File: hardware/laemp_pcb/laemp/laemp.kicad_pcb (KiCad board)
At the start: 2 copper layers, 1 part

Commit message: added new lib and schematic changes
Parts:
- moved A1 116.6 mm to (75.4, 92.8)

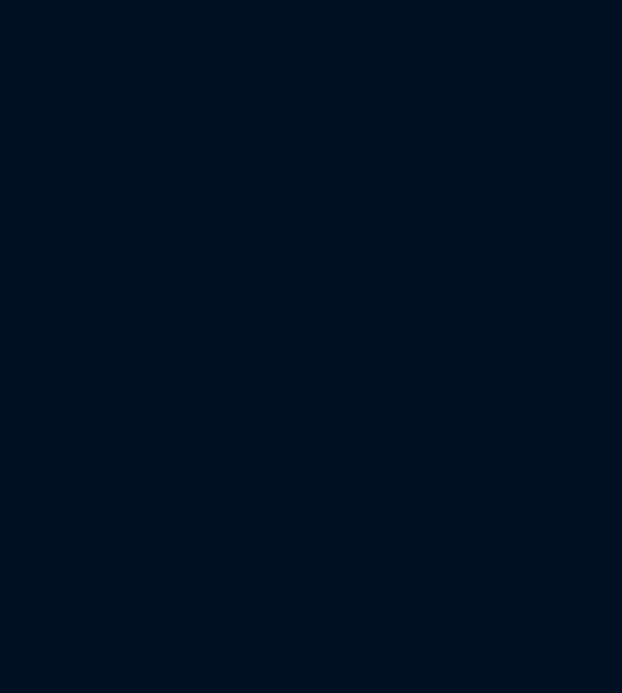
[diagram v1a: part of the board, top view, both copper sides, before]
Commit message: added 15V power supply and a total of 8 power LEDs
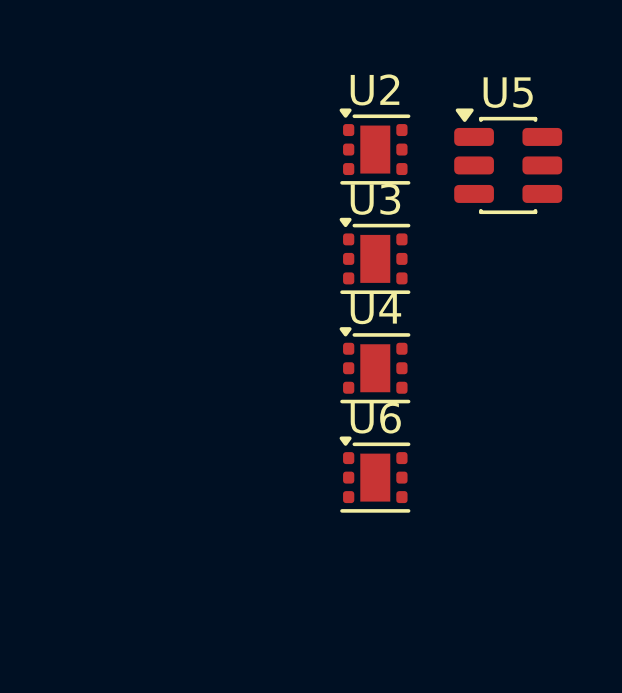
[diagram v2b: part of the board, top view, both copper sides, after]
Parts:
- added U2: TPS61165DRV, Package_SON:WSON-6-1EP_2x2mm_P0.65mm_EP1x1.6mm, F.Cu at (158.9, 63.9)
- added U3: TPS61165DRV, Package_SON:WSON-6-1EP_2x2mm_P0.65mm_EP1x1.6mm, F.Cu at (158.9, 67.5)
- added U4: TPS61165DRV, Package_SON:WSON-6-1EP_2x2mm_P0.65mm_EP1x1.6mm, F.Cu at (158.9, 71.2)
- added U5: TPS54202DDC, Package_TO_SOT_SMD:SOT-23-6, F.Cu at (163.3, 64.4)
- added U6: TPS61165DRV, Package_SON:WSON-6-1EP_2x2mm_P0.65mm_EP1x1.6mm, F.Cu at (158.9, 74.8)
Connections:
- A1 pad 13: Net-(A1-GND-Pad13) -> GND
- A1 pad 18: Net-(A1-GND-Pad13) -> GND
- A1 pad 23: Net-(A1-GND-Pad13) -> GND
- A1 pad 28: Net-(A1-GND-Pad13) -> GND
- A1 pad 3: Net-(A1-GND-Pad13) -> GND
- A1 pad 33: unconnected-(A1-AGND-Pad33) -> GND
- A1 pad 38: Net-(A1-GND-Pad13) -> GND
- A1 pad 39: unconnected-(A1-VSYS-Pad39) -> +5V
- A1 pad 8: Net-(A1-GND-Pad13) -> GND

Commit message: updated schematic
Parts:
- added C11: 4.7uF 50V X7R, Capacitor_SMD:C_0805_2012Metric, F.Cu at (105.5, 97.0)
- added C18: 220nF, Capacitor_SMD:C_0603_1608Metric, F.Cu at (109.7, 87.7)
- added C19: 220nF, Capacitor_SMD:C_0603_1608Metric, F.Cu at (109.7, 90.2)
- added C20: 220nF, Capacitor_SMD:C_0603_1608Metric, F.Cu at (109.7, 92.8)
- added C21: 220nF, Capacitor_SMD:C_0603_1608Metric, F.Cu at (109.7, 95.3)
- added C5: 4.7uF 50V X7R, Capacitor_SMD:C_0805_2012Metric, F.Cu at (105.5, 88.0)
- added C7: 4.7uF 50V X7R, Capacitor_SMD:C_0805_2012Metric, F.Cu at (105.5, 91.0)
- added C9: 4.7uF 50V X7R, Capacitor_SMD:C_0805_2012Metric, F.Cu at (105.5, 94.0)
- added R3: 0.56R, Resistor_SMD:R_1206_3216Metric, F.Cu at (100.4, 88.1)
- added R4: 0.62R, Resistor_SMD:R_1206_3216Metric, F.Cu at (100.4, 91.4)
- added R5: 0.62R, Resistor_SMD:R_1206_3216Metric, F.Cu at (100.4, 94.8)
- added R6: 0.62R, Resistor_SMD:R_1206_3216Metric, F.Cu at (100.4, 98.1)
- added U2: TPS61165DRV, Package_SON:WSON-6-1EP_2x2mm_P0.65mm_EP1x1.6mm, F.Cu at (113.5, 88.3)
- added U3: TPS61165DRV, Package_SON:WSON-6-1EP_2x2mm_P0.65mm_EP1x1.6mm, F.Cu at (113.5, 92.0)
- added U4: TPS61165DRV, Package_SON:WSON-6-1EP_2x2mm_P0.65mm_EP1x1.6mm, F.Cu at (113.5, 95.6)
- added U6: TPS61165DRV, Package_SON:WSON-6-1EP_2x2mm_P0.65mm_EP1x1.6mm, F.Cu at (113.5, 99.3)
- moved U2 56.9 mm to (102.6, 55.4)
- moved U3 56.9 mm to (102.6, 59.0)
- moved U4 56.9 mm to (102.6, 62.6)
- moved U5 56.9 mm to (107.0, 55.9)
- moved U6 56.9 mm to (102.6, 66.3)
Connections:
- A1 pad 33: GND -> AGND
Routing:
- added copper zone on B.Cu, net AGND
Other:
- board outline added: 100 x 100 mm
